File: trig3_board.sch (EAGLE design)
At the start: 97 parts, among them J1 2p-2.54, J10 2p-2.54, J11 2p-2.54, J12 2p-2.54, J13 8pin, J14 2p-2.54, J15 2p-2.54, J16 2p-2.54, J17 2p-2.54, J18 8pin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

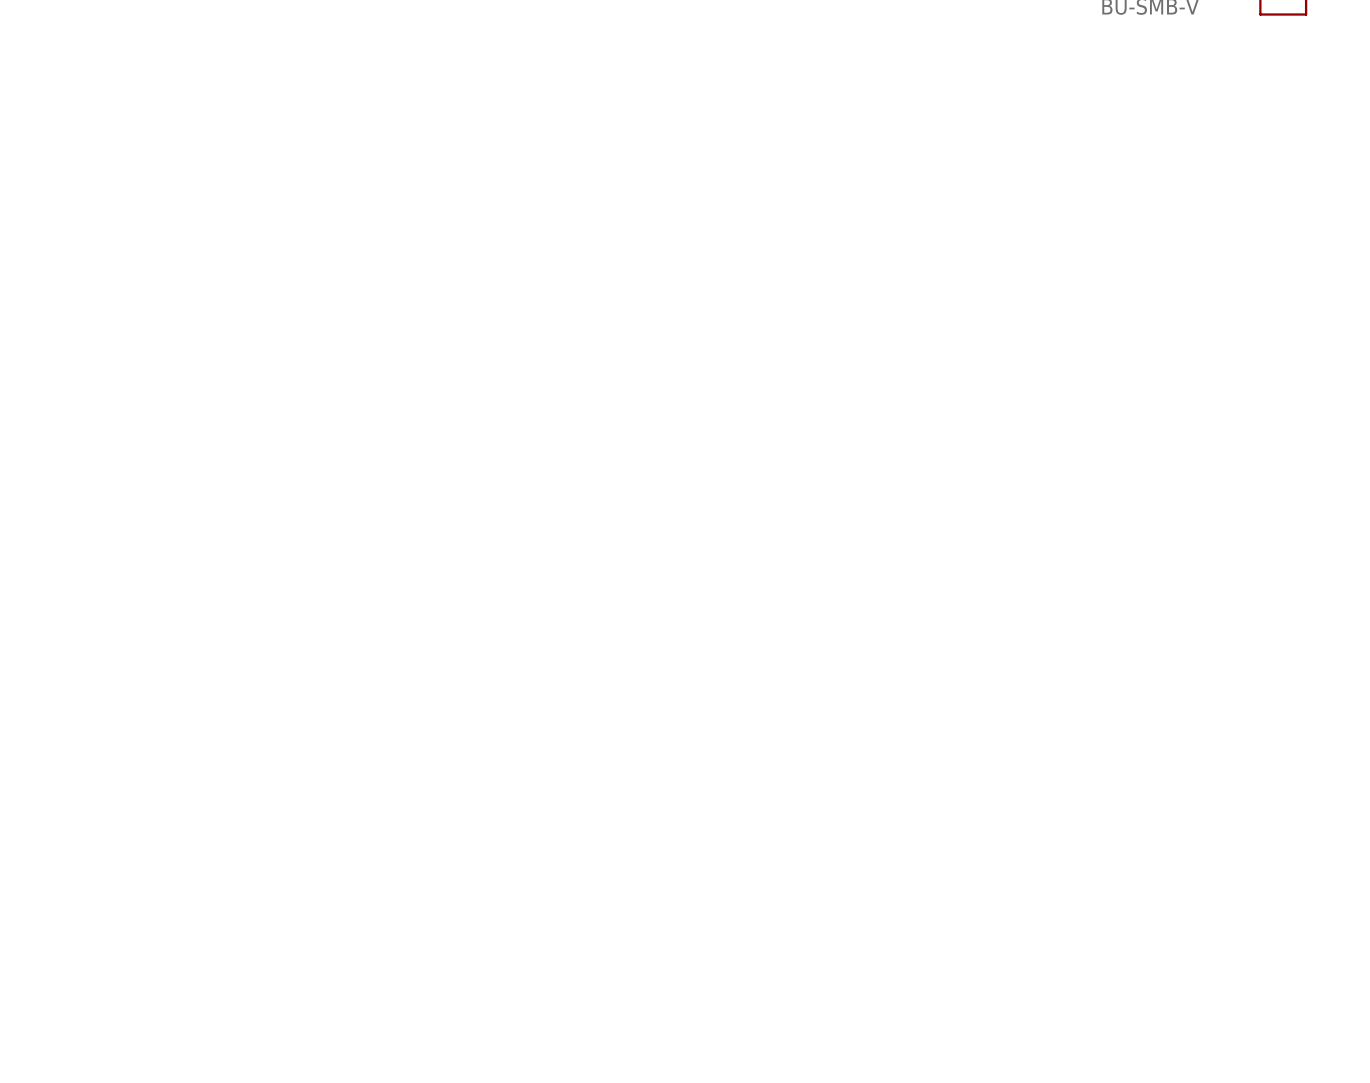
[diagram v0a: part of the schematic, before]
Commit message: VME board, ordered from JLCPCB
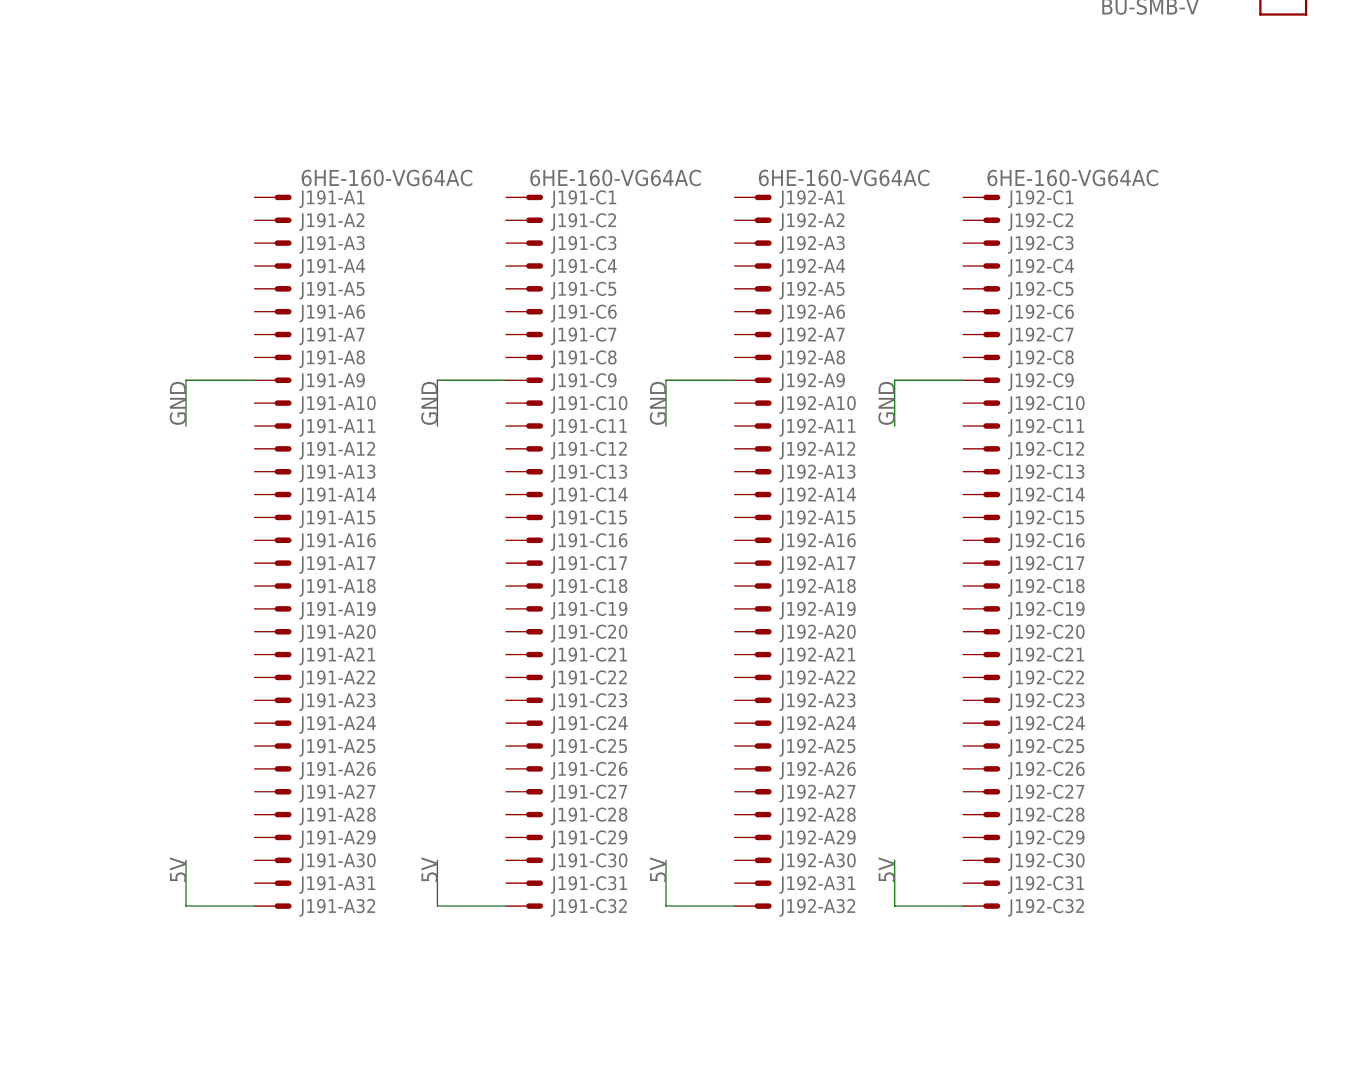
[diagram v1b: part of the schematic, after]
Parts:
- added J19: 6HE-160-VG64AC, 19inch:6HE-160-VG64AC
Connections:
- net 5V: now also J191-A32.MS, J191-C32.MS, J192-A32.MS, J192-C32.MS
- net GND: now also J191-A9.MS, J191-C9.MS, J192-A9.MS, J192-C9.MS
